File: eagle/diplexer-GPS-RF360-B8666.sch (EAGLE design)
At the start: 4 parts, among them U1 B8666, X1 SMA-142-0701-801/806, X2 SMA-142-0701-801/806, X3 SMA-142-0701-801/806

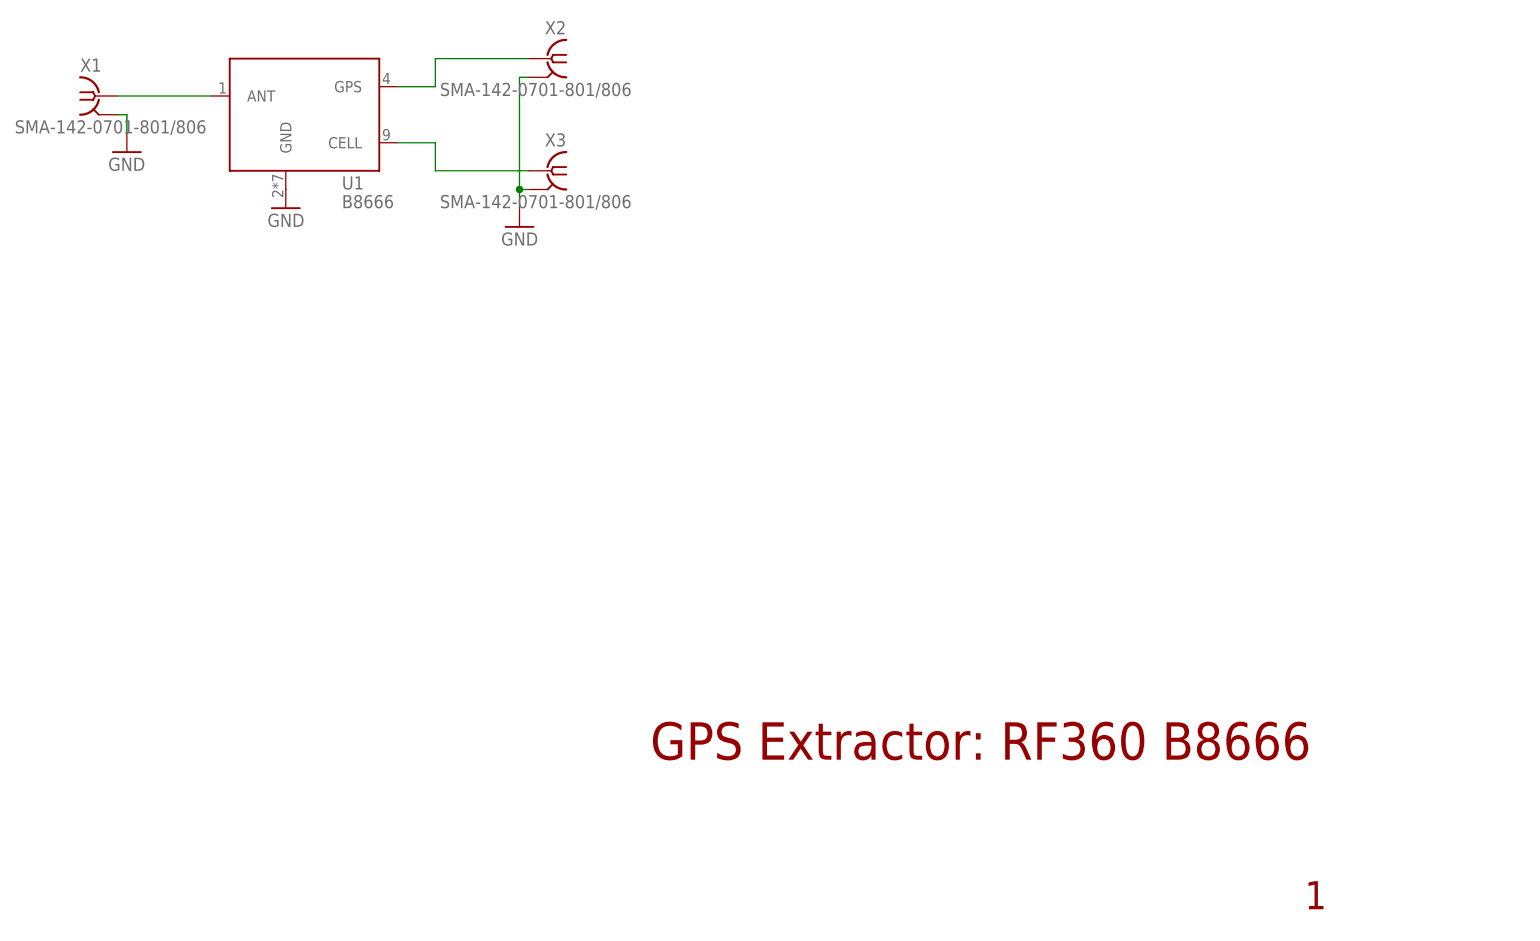
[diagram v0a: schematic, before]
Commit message: Add layout for GPS diplexer
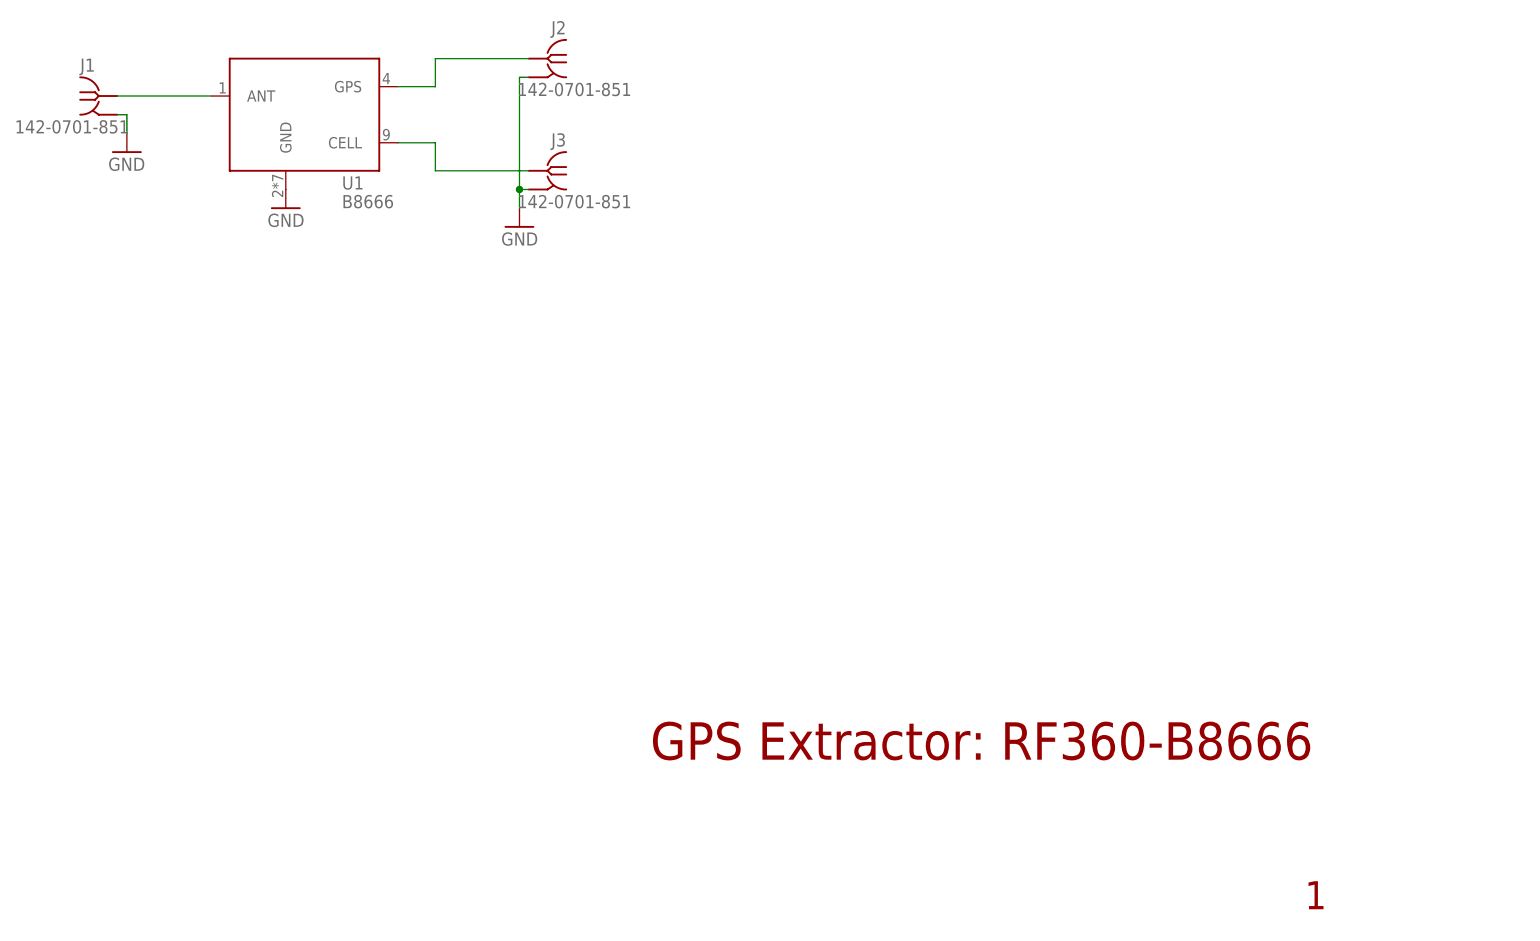
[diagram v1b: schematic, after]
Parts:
- removed X1, X2, X3: SMA-142-0701-801/806, con-coax:SMA-142-0701-801/806
- added J1, J2, J3: 142-0701-851, J-Cinch-142-0701-851-SMA-end-launch:142-0701-851
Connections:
- removed net N$1: U1.GPS, X2.1
- removed net N$2: U1.CELL, X3.1
- removed net N$57: U1.ANT, X1.1
- new net GPS: J2.RF, U1.GPS
- new net RF-IN: J1.RF, U1.ANT
- new net RF-OUT: J3.RF, U1.CELL
- net GND: now also J1.GND, J2.GND, J3.GND; no longer X1.2, X2.2, X3.2
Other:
- note added: "GPS Extractor: RF360-B8666"
- note removed: "GPS Extractor: RF360 B8666"
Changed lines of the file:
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@@
 <class number="0" name="default" width="0" drill="0">
+</class>
+<class number="1" name="RF" width="0" drill="0">
+<clearance class="1" value="0.7"/>
 </class>
 </classes>
@@
 <part name="FRAME2" library="frames" library_urn="urn:adsk.eagle:library:229" deviceset="FRAME_A_L" device=""/>
 <part name="U1" library="U-RF360-B8666-GPS-diplexer" deviceset="B8666" device=""/>
-<part name="X1" library="con-coax" library_urn="urn:adsk.eagle:library:133" deviceset="SMA-" device="142-0701-801/806" package3d_urn="urn:adsk.eagle:package:6214/1"/>
+<part name="J1" library="J-Cinch-142-0701-851-SMA-end-launch" deviceset="142-0701-851" device=""/>
 <part name="GND31" library="supply1" library_urn="urn:adsk.eagle:library:371" deviceset="GND" device=""/>
-<part name="X2" library="con-coax" library_urn="urn:adsk.eagle:library:133" deviceset="SMA-" device="142-0701-801/806" package3d_urn="urn:adsk.eagle:package:6214/1"/>
-<part name="X3" library="con-coax" library_urn="urn:adsk.eagle:library:133" deviceset="SMA-" device="142-0701-801/806" package3d_urn="urn:adsk.eagle:package:6214/1"/>
+<part name="J2" library="J-Cinch-142-0701-851-SMA-end-launch" deviceset="142-0701-851" device=""/>
+<part name="J3" library="J-Cinch-142-0701-851-SMA-end-launch" deviceset="142-0701-851" device=""/>
 <part name="GND2" library="supply1" library_urn="urn:adsk.eagle:library:371" deviceset="GND" device=""/>
 <part name="GND1" library="supply1" library_urn="urn:adsk.eagle:library:371" deviceset="GND" device=""/>
@@
 <sheet>
 <plain>
-<text x="176.53" y="26.67" size="5.08" layer="94">GPS Extractor: RF360 B8666</text>
+<text x="176.53" y="26.67" size="5.08" layer="94">GPS Extractor: RF360-B8666</text>
 <text x="265.43" y="6.35" size="3.81" layer="94">1</text>
 </plain>
@@
 <attribute name="VALUE" x="134.62" y="101.6" size="1.778" layer="96"/>
 </instance>
-<instance part="X1" gate="G1" x="101.6" y="116.84" smashed="yes">
+<instance part="J1" gate="G$1" x="101.6" y="116.84" smashed="yes">
 <attribute name="VALUE" x="90.17" y="111.76" size="1.778" layer="96"/>
 <attribute name="NAME" x="99.06" y="120.142" size="1.778" layer="95"/>
@@
 <attribute name="VALUE" x="102.87" y="106.68" size="1.778" layer="96"/>
 </instance>
-<instance part="X2" gate="G1" x="162.56" y="121.92" smashed="yes" rot="MR0">
+<instance part="J2" gate="G$1" x="162.56" y="121.92" smashed="yes" rot="MR0">
 <attribute name="VALUE" x="173.99" y="116.84" size="1.778" layer="96" rot="MR0"/>
 <attribute name="NAME" x="165.1" y="125.222" size="1.778" layer="95" rot="MR0"/>
 </instance>
-<instance part="X3" gate="G1" x="162.56" y="106.68" smashed="yes" rot="MR0">
+<instance part="J3" gate="G$1" x="162.56" y="106.68" smashed="yes" rot="MR0">
 <attribute name="VALUE" x="173.99" y="101.6" size="1.778" layer="96" rot="MR0"/>
 <attribute name="NAME" x="165.1" y="109.982" size="1.778" layer="95" rot="MR0"/>
@@
 <net name="GND" class="0">
 <segment>
-<pinref part="X1" gate="G1" pin="2"/>
+<pinref part="J1" gate="G$1" pin="GND"/>
 <pinref part="GND31" gate="1" pin="GND"/>
 <wire x1="104.14" y1="114.3" x2="105.41" y2="114.3" width="0.1524" layer="91"/>
@@
 </segment>
 <segment>
-<pinref part="X3" gate="G1" pin="2"/>
+<pinref part="J3" gate="G$1" pin="GND"/>
 <pinref part="GND2" gate="1" pin="GND"/>
 <wire x1="160.02" y1="104.14" x2="158.75" y2="104.14" width="0.1524" layer="91"/>
 <wire x1="158.75" y1="104.14" x2="158.75" y2="101.6" width="0.1524" layer="91"/>
-<pinref part="X2" gate="G1" pin="2"/>
+<pinref part="J2" gate="G$1" pin="GND"/>
 <wire x1="160.02" y1="119.38" x2="158.75" y2="119.38" width="0.1524" layer="91"/>
 <wire x1="158.75" y1="104.14" x2="158.75" y2="119.38" width="0.1524" layer="91"/>
@@
 </segment>
 </net>
-<net name="N$57" class="0">
+<net name="RF-IN" class="1">
 <segment>
-<pinref part="X1" gate="G1" pin="1"/>
+<pinref part="J1" gate="G$1" pin="RF"/>
 <wire x1="104.14" y1="116.84" x2="116.84" y2="116.84" width="0.1524" layer="91"/>
 <pinref part="U1" gate="G$1" pin="ANT"/>
 </segment>
 </net>
-<net name="N$1" class="0">
+<net name="GPS" class="1">
 <segment>
-<pinref part="X2" gate="G1" pin="1"/>
+<pinref part="J2" gate="G$1" pin="RF"/>
 <wire x1="160.02" y1="121.92" x2="147.32" y2="121.92" width="0.1524" layer="91"/>
 <pinref part="U1" gate="G$1" pin="GPS"/>
@@
 </segment>
 </net>
-<net name="N$2" class="0">
+<net name="RF-OUT" class="1">
 <segment>
-<pinref part="X3" gate="G1" pin="1"/>
+<pinref part="J3" gate="G$1" pin="RF"/>
 <wire x1="160.02" y1="106.68" x2="147.32" y2="106.68" width="0.1524" layer="91"/>
 <pinref part="U1" gate="G$1" pin="CELL"/>
@@
 will not be understood (or retained) with this version.
 </note>
-<note version="8.3" severity="warning">
-Since Version 8.3, EAGLE supports the association of 3D packages
-with devices in libraries, schematics, and board files. Those 3D
-packages will not be understood (or retained) with this version.
-</note>
 </compatibility>
